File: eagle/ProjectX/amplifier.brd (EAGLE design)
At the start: 100 x 80 mm, 8 parts, among them U1 TC4427COA, U2 TC4427COA

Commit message: Some work on the final design
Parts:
- removed C3: 4.7uF, rcl:C0805
- removed C4: 100nF, rcl:C0805
- moved C2 15.1 mm to (72.7, 39.7)
- moved C1 14.3 mm to (72.7, 37.7)
- moved U1 5.63 mm to (74.8, 46.4), turned to 270 degrees
- moved SV2 5.47 mm to (53.3, 53.5)
- moved U2 2.55 mm to (71.6, 31.0), turned to 270 degrees
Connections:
- net GND: now also U1.1, U2.1; no longer C3.2, C4.2
- net VCC: now also U1.8, U2.8; no longer C3.1, C4.1
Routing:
- net N$4: track 21.4 -> 6.77 mm
- net GND: track 41.8 -> 29.7 mm
- net N$5: track 17.3 -> 6.77 mm
- net VCC: track 41.8 -> 31.3 mm
- net N$6: track 32.1 -> 22.9 mm
- net N$8: track 12.0 -> 3.35 mm
- net N$2: track 25.5 -> 19.5 mm
- net N$7: track 9.25 -> 3.35 mm
- net N$1: track 26.8 -> 22.4 mm
- net N$3: track 20.8 -> 19.5 mm

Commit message: More work on the 32 bit board
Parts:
- added C10, C12, C18, C20, C26, C28, C6: 100nF, rcl:C0805
- added C11, C17, C19, C25, C27, C5, C9: 4.7uF, rcl:C0805
- added U10, U11, U12, U17, U18, U19, U20, U25, U26, U27, U28, U5, U6, U9: TC4427COA, Microchip_By_element14_Batch_1:SOIC127P600X175-8N
- SV1, SV2: device con-lstb:MA20-2W -> Parts:MA20-2W
- moved U2 53.0 mm to (18.7, 32.0)
- moved C1 52.6 mm to (20.2, 40.5)
- moved C2 52.5 mm to (20.2, 38.5)
- moved U1 51.9 mm to (23.0, 46.2)
- moved SV1 9.36 mm to (59.3, 16.9)
- moved SV2 8.38 mm to (59.2, 59.4)
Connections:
- new net N$10: SV1.1, U2.7
- new net N$100: SV1.25, U26.7
- new net N$101: SV1.26, U26.5
- new net N$102: SV2.25, U26.2
- new net N$103: SV1.27, U25.7
- new net N$104: SV1.28, U25.5
- new net N$105: SV2.30, U27.4
- new net N$106: SV2.29, U27.2
- new net N$107: SV2.32, U28.4
- new net N$108: SV1.31, U28.7
- new net N$109: SV1.32, U28.5
- new net N$11: SV1.3, U1.7
- new net N$110: SV2.31, U28.2
- new net N$111: SV1.29, U27.7
- new net N$112: SV1.30, U27.5
- new net N$12: SV1.7, U6.7
- new net N$13: SV1.10, U10.5
- new net N$14: SV1.9, U10.7
- new net N$15: SV1.11, U9.7
- new net N$16: SV1.23, U20.7
- new net N$17: SV2.6, U5.4
- new net N$18: SV2.5, U5.2
- new net N$19: SV2.8, U6.4
- new net N$22: SV2.7, U6.2
- new net N$23: SV1.5, U5.7
- new net N$24: SV1.6, U5.5
- new net N$26: SV1.15, U12.7
- new net N$29: SV1.12, U9.5
- new net N$33: SV2.12, U9.4
- new net N$34: SV2.11, U9.2
- new net N$35: SV2.10, U10.4
- new net N$38: SV2.9, U10.2
- new net N$41: SV2.14, U11.4
- new net N$42: SV2.13, U11.2
- new net N$43: SV2.16, U12.4
- new net N$46: SV2.15, U12.2
- new net N$47: SV1.13, U11.7
- new net N$48: SV1.14, U11.5
- new net N$65: SV2.20, U17.4
- new net N$66: SV2.19, U17.2
- new net N$67: SV2.18, U18.4
- new net N$68: SV1.17, U18.7
- new net N$69: SV1.18, U18.5
- new net N$70: SV2.17, U18.2
- new net N$71: SV1.19, U17.7
- new net N$72: SV1.20, U17.5
- new net N$73: SV2.22, U19.4
- new net N$74: SV2.21, U19.2
- new net N$75: SV2.24, U20.4
- new net N$78: SV2.23, U20.2
- new net N$79: SV1.21, U19.7
- new net N$80: SV1.22, U19.5
- new net N$9: SV1.8, U6.5
- new net N$97: SV2.28, U25.4
- new net N$98: SV2.27, U25.2
- new net N$99: SV2.26, U26.4
- net GND: now also C10.2, C11.2, C12.2, C17.2, C18.2, C19.2, C20.2, C25.2, C26.2, C27.2, C28.2, C5.2, C6.2, C9.2, U10.1, U10.3, U11.1, U11.3, U12.1, U12.3, U17.1, U17.3, U18.1, U18.3, U19.1, U19.3, U20.1, U20.3, U25.1, U25.3, U26.1, U26.3, U27.1, U27.3, U28.1, U28.3, U5.1, U5.3, U6.1, U6.3, U9.1, U9.3; no longer SV1.1, SV1.2, SV2.1, SV2.2
- net N$1: now also SV2.2; no longer SV2.34
- net N$2: now also SV1.2, U2.5; no longer SV1.39, U1.7
- net N$3: now also SV1.4; no longer SV1.37
- net N$4: now also SV2.4; no longer SV2.38
- net N$5: now also SV2.3; no longer SV2.40
- net N$6: now also SV2.1; no longer SV2.36
- net N$7: now also SV1.16, U12.5; no longer SV1.35, U2.7
- net N$8: now also SV1.24, U20.5; no longer SV1.33, U2.5
- net VCC: now also C10.1, C11.1, C12.1, C17.1, C18.1, C19.1, C20.1, C25.1, C26.1, C27.1, C28.1, C5.1, C6.1, C9.1, U10.6, U10.8, U11.6, U11.8, U12.6, U12.8, U17.6, U17.8, U18.6, U18.8, U19.6, U19.8, U20.6, U20.8, U25.6, U25.8, U26.6, U26.8, U27.6, U27.8, U28.6, U28.8, U5.6, U5.8, U6.6, U6.8, U9.6, U9.8; no longer SV1.3, SV1.4, SV2.3, SV2.4
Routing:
- net GND: track 29.7 -> 333.3 mm
- net VCC: track 31.3 -> 321.0 mm
- net N$104: track 0.00 -> 40.6 mm
- net N$112: track 0.00 -> 40.3 mm
- net N$24: track 0.00 -> 38.9 mm
- net N$111: track 0.00 -> 38.0 mm
- net N$23: track 0.00 -> 37.1 mm
- net N$103: track 0.00 -> 36.6 mm
- net N$11: track 0.00 -> 34.7 mm
- net N$80: track 0.00 -> 32.6 mm
- net N$48: track 0.00 -> 32.0 mm
- net N$29: track 0.00 -> 31.5 mm
- net N$72: track 0.00 -> 31.3 mm
- net N$47: track 0.00 -> 30.3 mm
- net N$79: track 0.00 -> 29.6 mm
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
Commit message: Added a finished board
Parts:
- added D1: (no value), SparkFun-LED:LED-0603
- added J1, J2: (no value), SparkFun-Connectors:1X02_LONGPADS
- added R1: 1k, SparkFun-Resistors:0805
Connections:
- removed net VCC: C1.1, C10.1, C11.1, C12.1, C17.1, C18.1, C19.1, C2.1, C20.1, C25.1, C26.1, C27.1, C28.1, C5.1, C6.1, C9.1, U1.6, U1.8, U10.6, U10.8, U11.6, U11.8, U12.6, U12.8, U17.6, U17.8, U18.6, U18.8, U19.6, U19.8, U2.6, U2.8, U20.6, U20.8, U25.6, U25.8, U26.6, U26.8, U27.6, U27.8, U28.6, U28.8, U5.6, U5.8, U6.6, U6.8, U9.6, U9.8
- new net N$20: D1.A, R1.1
- new net VDD: C1.1, C10.1, C11.1, C12.1, C17.1, C18.1, C19.1, C2.1, C20.1, C25.1, C26.1, C27.1, C28.1, C5.1, C6.1, C9.1, J1.1, J2.1, R1.2, U1.6, U1.8, U10.6, U10.8, U11.6, U11.8, U12.6, U12.8, U17.6, U17.8, U18.6, U18.8, U19.6, U19.8, U2.6, U2.8, U20.6, U20.8, U25.6, U25.8, U26.6, U26.8, U27.6, U27.8, U28.6, U28.8, U5.6, U5.8, U6.6, U6.8, U9.6, U9.8
- net GND: now also D1.C, J1.2, J2.2, SV1.GND, SV1.GND+1, SV2.GND, SV2.GND+1
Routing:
- net VDD: track 0.00 -> 337.0 mm
- net VCC: track 321.0 -> 0.00 mm
- net N$1: track 14.0 -> 40.8 mm
- net N$4: track 0.00 -> 25.7 mm
- net N$107: track 16.7 -> 42.0 mm
- net N$6: track 15.0 -> 38.3 mm
- net N$105: track 0.00 -> 23.2 mm
- net N$110: track 15.7 -> 37.9 mm
- net N$106: track 0.00 -> 22.2 mm
- net N$17: track 0.00 -> 21.0 mm
- net N$5: track 0.00 -> 21.0 mm
- net N$97: track 0.00 -> 19.5 mm
- net N$98: track 0.00 -> 18.9 mm
- net N$99: track 14.0 -> 31.9 mm
- net N$18: track 0.00 -> 17.4 mm
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- added copper zone on layer 1, net GND
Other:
- board size 100 x 80 mm -> 93.6 x 54 mm

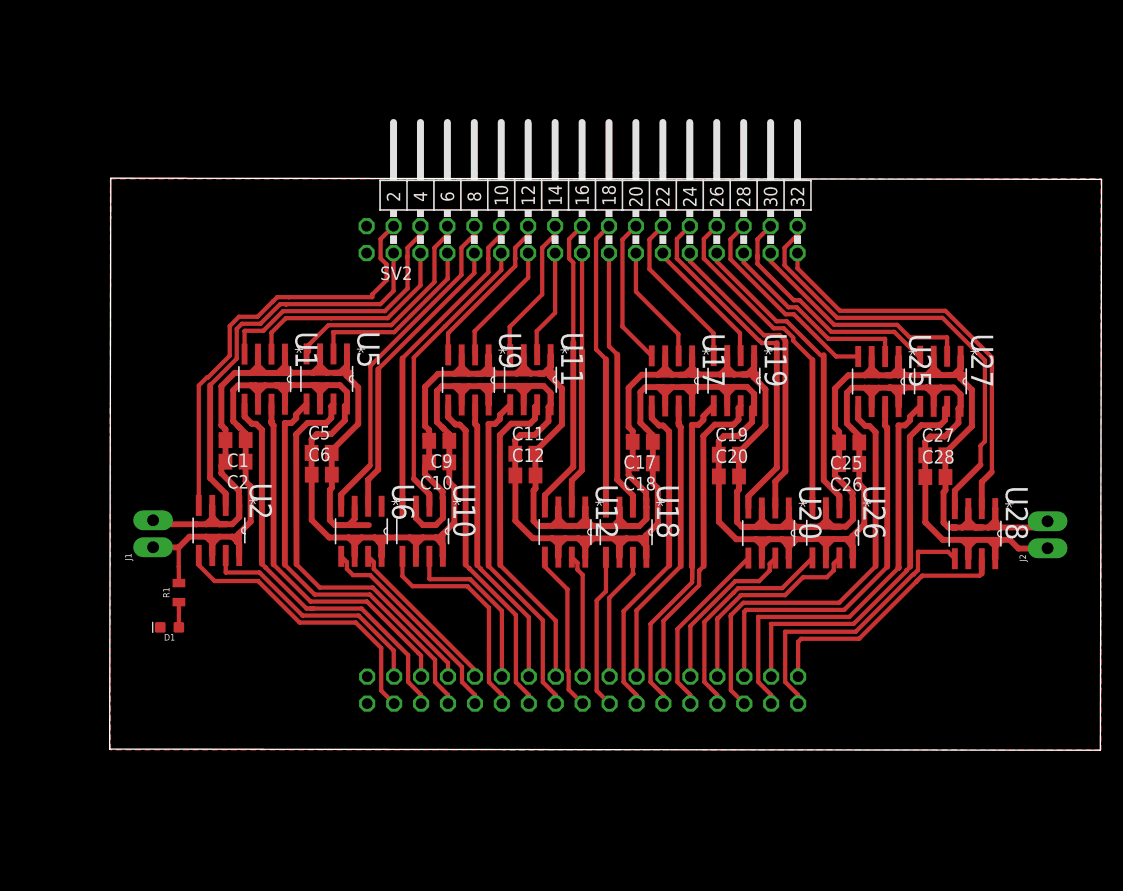
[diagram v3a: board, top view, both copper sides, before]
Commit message: Finished the small amplifier board
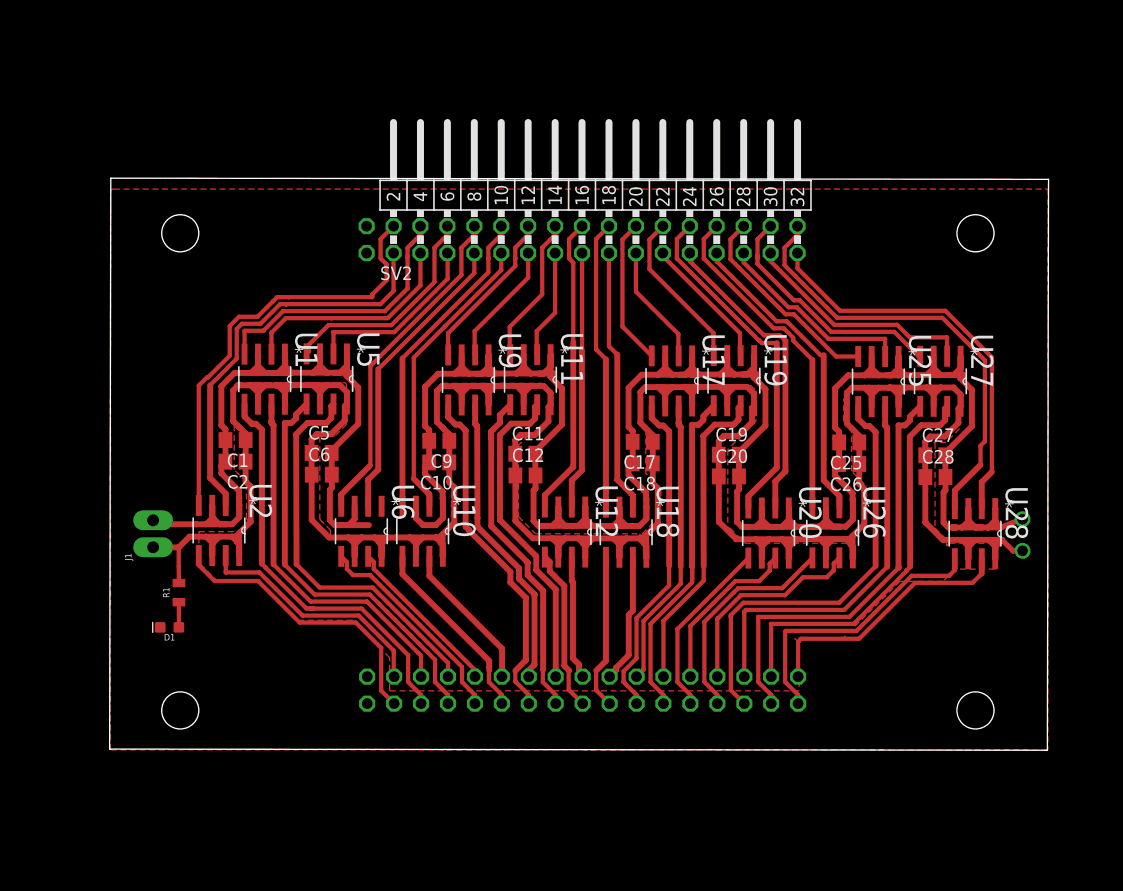
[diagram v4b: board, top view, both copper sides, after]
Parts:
- removed J2: (no value), SparkFun-Connectors:1X02_LONGPADS
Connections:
- net GND: no longer J2.2
- net VDD: no longer J2.1
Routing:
- net N$13: track 20.8 -> 18.1 mm
- net GND: track 329.1 -> 326.6 mm, vias 0 -> 1
- net VDD: track 337.0 -> 334.7 mm, vias 0 -> 1
- net N$14: track 16.4 -> 14.2 mm
- net N$109: track 27.7 -> 26.8 mm
- net N$29: track 31.5 -> 32.4 mm
- net N$48: track 32.0 -> 31.5 mm
- added copper zone on layer 1, net VDD
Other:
- board size 93.6 x 54 mm -> 88.6 x 54 mm

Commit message: changes
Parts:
- removed C10, C12, C18, C20, C26, C28, C6: 100nF, rcl:C0805
- removed C11, C17, C19, C25, C27, C5, C9: 4.7uF, rcl:C0805
- removed D1: (no value), SparkFun-LED:LED-0603
- removed J1: (no value), SparkFun-Connectors:1X02_LONGPADS
- removed R1: 1k, SparkFun-Resistors:0805
- removed U10, U11, U12, U17, U18, U19, U20, U25, U26, U27, U28, U5, U6, U9: TC4427COA, Microchip_By_element14_Batch_1:SOIC127P600X175-8N
- added C3: 4.7uF, rcl:C0805
- added C4: 100nF, rcl:C0805
- SV1, SV2: device Parts:MA20-2W -> con-lstb:MA20-2W
- moved C2 60.2 mm to (80.0, 45.7)
- moved C1 59.9 mm to (80.0, 43.4)
- moved U1 56.9 mm to (79.8, 50.0), turned to 0 degrees
- moved U2 54.9 mm to (72.4, 43.2), turned to 180 degrees
- moved SV1 9.36 mm to (53.3, 24.1)
- moved SV2 5.92 mm to (53.3, 58.9)
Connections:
- removed net N$10: SV1.1, U2.7
- removed net N$100: SV1.25, U26.7
- removed net N$101: SV1.26, U26.5
- removed net N$102: SV2.25, U26.2
- removed net N$103: SV1.27, U25.7
- removed net N$104: SV1.28, U25.5
- removed net N$105: SV2.30, U27.4
- removed net N$106: SV2.29, U27.2
- removed net N$107: SV2.32, U28.4
- removed net N$108: SV1.31, U28.7
- removed net N$109: SV1.32, U28.5
- removed net N$11: SV1.3, U1.7
- removed net N$110: SV2.31, U28.2
- removed net N$111: SV1.29, U27.7
- removed net N$112: SV1.30, U27.5
- removed net N$12: SV1.7, U6.7
- removed net N$13: SV1.10, U10.5
- removed net N$14: SV1.9, U10.7
- removed net N$15: SV1.11, U9.7
- removed net N$16: SV1.23, U20.7
- removed net N$17: SV2.6, U5.4
- removed net N$18: SV2.5, U5.2
- removed net N$19: SV2.8, U6.4
- removed net N$20: D1.A, R1.1
- removed net N$22: SV2.7, U6.2
- removed net N$23: SV1.5, U5.7
- removed net N$24: SV1.6, U5.5
- removed net N$26: SV1.15, U12.7
- removed net N$29: SV1.12, U9.5
- removed net N$33: SV2.12, U9.4
- removed net N$34: SV2.11, U9.2
- removed net N$35: SV2.10, U10.4
- removed net N$38: SV2.9, U10.2
- removed net N$41: SV2.14, U11.4
- removed net N$42: SV2.13, U11.2
- removed net N$43: SV2.16, U12.4
- removed net N$46: SV2.15, U12.2
- removed net N$47: SV1.13, U11.7
- removed net N$48: SV1.14, U11.5
- removed net N$65: SV2.20, U17.4
- removed net N$66: SV2.19, U17.2
- removed net N$67: SV2.18, U18.4
- removed net N$68: SV1.17, U18.7
- removed net N$69: SV1.18, U18.5
- removed net N$70: SV2.17, U18.2
- removed net N$71: SV1.19, U17.7
- removed net N$72: SV1.20, U17.5
- removed net N$73: SV2.22, U19.4
- removed net N$74: SV2.21, U19.2
- removed net N$75: SV2.24, U20.4
- removed net N$78: SV2.23, U20.2
- removed net N$79: SV1.21, U19.7
- removed net N$80: SV1.22, U19.5
- removed net N$9: SV1.8, U6.5
- removed net N$97: SV2.28, U25.4
- removed net N$98: SV2.27, U25.2
- removed net N$99: SV2.26, U26.4
- removed net VDD: C1.1, C10.1, C11.1, C12.1, C17.1, C18.1, C19.1, C2.1, C20.1, C25.1, C26.1, C27.1, C28.1, C5.1, C6.1, C9.1, J1.1, R1.2, U1.6, U1.8, U10.6, U10.8, U11.6, U11.8, U12.6, U12.8, U17.6, U17.8, U18.6, U18.8, U19.6, U19.8, U2.6, U2.8, U20.6, U20.8, U25.6, U25.8, U26.6, U26.8, U27.6, U27.8, U28.6, U28.8, U5.6, U5.8, U6.6, U6.8, U9.6, U9.8
- new net VCC: C1.1, C2.1, C3.1, C4.1, SV1.3, SV1.4, SV2.3, SV2.4, U1.6, U2.6
- net GND: now also C3.2, C4.2, SV1.1, SV1.2, SV2.1, SV2.2; no longer C10.2, C11.2, C12.2, C17.2, C18.2, C19.2, C20.2, C25.2, C26.2, C27.2, C28.2, C5.2, C6.2, C9.2, D1.C, J1.2, SV1.GND, SV1.GND+1, SV2.GND, SV2.GND+1, U1.1, U10.1, U10.3, U11.1, U11.3, U12.1, U12.3, U17.1, U17.3, U18.1, U18.3, U19.1, U19.3, U2.1, U20.1, U20.3, U25.1, U25.3, U26.1, U26.3, U27.1, U27.3, U28.1, U28.3, U5.1, U5.3, U6.1, U6.3, U9.1, U9.3
- net N$1: now also SV2.34; no longer SV2.2
- net N$2: now also SV1.39, U1.7; no longer SV1.2, U2.5
- net N$3: now also SV1.37; no longer SV1.4
- net N$4: now also SV2.38; no longer SV2.4
- net N$5: now also SV2.40; no longer SV2.3
- net N$6: now also SV2.36; no longer SV2.1
- net N$7: now also SV1.35, U2.7; no longer SV1.16, U12.5
- net N$8: now also SV1.33, U2.5; no longer SV1.24, U20.5
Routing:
- net VDD: track 334.7 -> 0.00 mm, vias 1 -> 0
- net GND: track 326.6 -> 0.00 mm, vias 1 -> 0
- net N$107: track 42.0 -> 0.00 mm
- net N$1: track 40.8 -> 0.00 mm
- net N$104: track 40.6 -> 0.00 mm
- net N$112: track 40.3 -> 0.00 mm
- net N$24: track 38.9 -> 0.00 mm
- net N$3: track 38.7 -> 0.00 mm
- net N$6: track 38.3 -> 0.00 mm
- net N$111: track 38.0 -> 0.00 mm
- net N$110: track 37.9 -> 0.00 mm
- net N$23: track 37.1 -> 0.00 mm
- net N$103: track 36.6 -> 0.00 mm
- net N$11: track 34.7 -> 0.00 mm
- net N$75: track 33.0 -> 0.00 mm
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- removed copper zone on layer 1, net GND
- removed copper zone on layer 1, net VDD
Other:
- board size 88.6 x 54 mm -> 100 x 80 mm

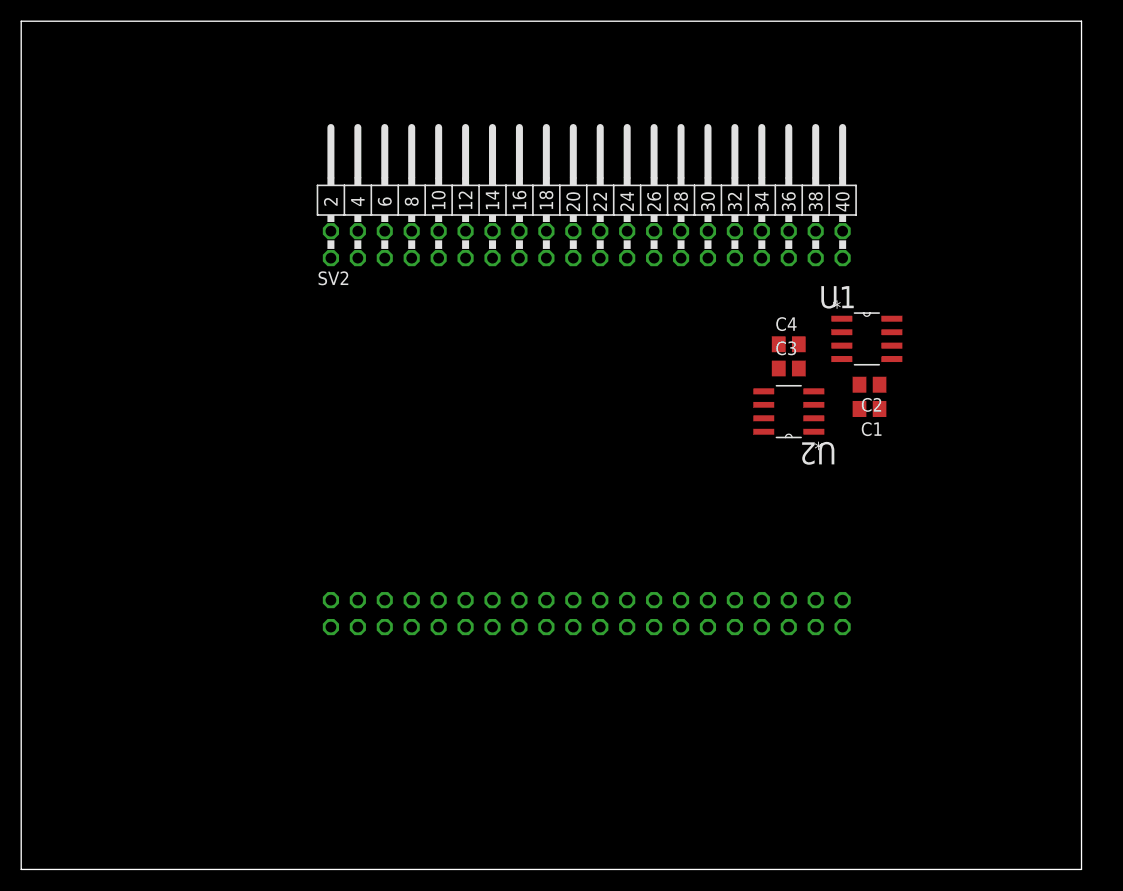
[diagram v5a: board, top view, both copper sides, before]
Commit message: Restored the eagle work to the last working copy
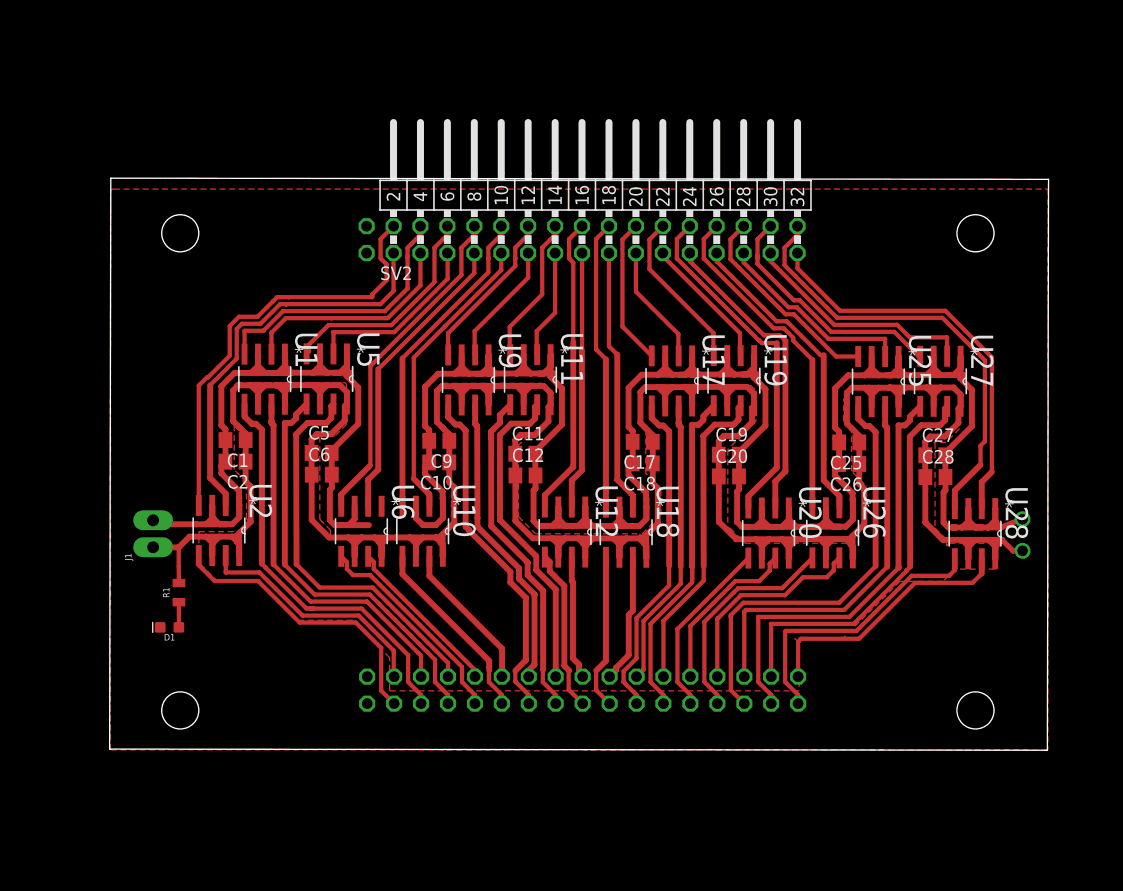
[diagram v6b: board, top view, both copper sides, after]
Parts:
- removed C3: 4.7uF, rcl:C0805
- removed C4: 100nF, rcl:C0805
- added C10, C12, C18, C20, C26, C28, C6: 100nF, rcl:C0805
- added C11, C17, C19, C25, C27, C5, C9: 4.7uF, rcl:C0805
- added D1: (no value), SparkFun-LED:LED-0603
- added J1: (no value), SparkFun-Connectors:1X02_LONGPADS
- added R1: 1k, SparkFun-Resistors:0805
- added U10, U11, U12, U17, U18, U19, U20, U25, U26, U27, U28, U5, U6, U9: TC4427COA, Microchip_By_element14_Batch_1:SOIC127P600X175-8N
- SV1, SV2: device con-lstb:MA20-2W -> Parts:MA20-2W
- moved C2 60.2 mm to (20.2, 38.5)
- moved C1 59.9 mm to (20.2, 40.5)
- moved U1 56.9 mm to (23.0, 46.2), turned to 270 degrees
- moved U2 54.9 mm to (18.7, 32.0), turned to 270 degrees
- moved SV1 9.36 mm to (59.3, 16.9)
- moved SV2 5.92 mm to (59.2, 59.4)
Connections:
- removed net VCC: C1.1, C2.1, C3.1, C4.1, SV1.3, SV1.4, SV2.3, SV2.4, U1.6, U2.6
- new net N$10: SV1.1, U2.7
- new net N$100: SV1.25, U26.7
- new net N$101: SV1.26, U26.5
- new net N$102: SV2.25, U26.2
- new net N$103: SV1.27, U25.7
- new net N$104: SV1.28, U25.5
- new net N$105: SV2.30, U27.4
- new net N$106: SV2.29, U27.2
- new net N$107: SV2.32, U28.4
- new net N$108: SV1.31, U28.7
- new net N$109: SV1.32, U28.5
- new net N$11: SV1.3, U1.7
- new net N$110: SV2.31, U28.2
- new net N$111: SV1.29, U27.7
- new net N$112: SV1.30, U27.5
- new net N$12: SV1.7, U6.7
- new net N$13: SV1.10, U10.5
- new net N$14: SV1.9, U10.7
- new net N$15: SV1.11, U9.7
- new net N$16: SV1.23, U20.7
- new net N$17: SV2.6, U5.4
- new net N$18: SV2.5, U5.2
- new net N$19: SV2.8, U6.4
- new net N$20: D1.A, R1.1
- new net N$22: SV2.7, U6.2
- new net N$23: SV1.5, U5.7
- new net N$24: SV1.6, U5.5
- new net N$26: SV1.15, U12.7
- new net N$29: SV1.12, U9.5
- new net N$33: SV2.12, U9.4
- new net N$34: SV2.11, U9.2
- new net N$35: SV2.10, U10.4
- new net N$38: SV2.9, U10.2
- new net N$41: SV2.14, U11.4
- new net N$42: SV2.13, U11.2
- new net N$43: SV2.16, U12.4
- new net N$46: SV2.15, U12.2
- new net N$47: SV1.13, U11.7
- new net N$48: SV1.14, U11.5
- new net N$65: SV2.20, U17.4
- new net N$66: SV2.19, U17.2
- new net N$67: SV2.18, U18.4
- new net N$68: SV1.17, U18.7
- new net N$69: SV1.18, U18.5
- new net N$70: SV2.17, U18.2
- new net N$71: SV1.19, U17.7
- new net N$72: SV1.20, U17.5
- new net N$73: SV2.22, U19.4
- new net N$74: SV2.21, U19.2
- new net N$75: SV2.24, U20.4
- new net N$78: SV2.23, U20.2
- new net N$79: SV1.21, U19.7
- new net N$80: SV1.22, U19.5
- new net N$9: SV1.8, U6.5
- new net N$97: SV2.28, U25.4
- new net N$98: SV2.27, U25.2
- new net N$99: SV2.26, U26.4
- new net VDD: C1.1, C10.1, C11.1, C12.1, C17.1, C18.1, C19.1, C2.1, C20.1, C25.1, C26.1, C27.1, C28.1, C5.1, C6.1, C9.1, J1.1, R1.2, U1.6, U1.8, U10.6, U10.8, U11.6, U11.8, U12.6, U12.8, U17.6, U17.8, U18.6, U18.8, U19.6, U19.8, U2.6, U2.8, U20.6, U20.8, U25.6, U25.8, U26.6, U26.8, U27.6, U27.8, U28.6, U28.8, U5.6, U5.8, U6.6, U6.8, U9.6, U9.8
- net GND: now also C10.2, C11.2, C12.2, C17.2, C18.2, C19.2, C20.2, C25.2, C26.2, C27.2, C28.2, C5.2, C6.2, C9.2, D1.C, J1.2, SV1.GND, SV1.GND+1, SV2.GND, SV2.GND+1, U1.1, U10.1, U10.3, U11.1, U11.3, U12.1, U12.3, U17.1, U17.3, U18.1, U18.3, U19.1, U19.3, U2.1, U20.1, U20.3, U25.1, U25.3, U26.1, U26.3, U27.1, U27.3, U28.1, U28.3, U5.1, U5.3, U6.1, U6.3, U9.1, U9.3; no longer C3.2, C4.2, SV1.1, SV1.2, SV2.1, SV2.2
- net N$1: now also SV2.2; no longer SV2.34
- net N$2: now also SV1.2, U2.5; no longer SV1.39, U1.7
- net N$3: now also SV1.4; no longer SV1.37
- net N$4: now also SV2.4; no longer SV2.38
- net N$5: now also SV2.3; no longer SV2.40
- net N$6: now also SV2.1; no longer SV2.36
- net N$7: now also SV1.16, U12.5; no longer SV1.35, U2.7
- net N$8: now also SV1.24, U20.5; no longer SV1.33, U2.5
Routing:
- net VDD: track 0.00 -> 334.7 mm, vias 0 -> 1
- net GND: track 0.00 -> 326.6 mm, vias 0 -> 1
- net N$107: track 0.00 -> 42.0 mm
- net N$1: track 0.00 -> 40.8 mm
- net N$104: track 0.00 -> 40.6 mm
- net N$112: track 0.00 -> 40.3 mm
- net N$24: track 0.00 -> 38.9 mm
- net N$3: track 0.00 -> 38.7 mm
- net N$6: track 0.00 -> 38.3 mm
- net N$111: track 0.00 -> 38.0 mm
- net N$110: track 0.00 -> 37.9 mm
- net N$23: track 0.00 -> 37.1 mm
- net N$103: track 0.00 -> 36.6 mm
- net N$11: track 0.00 -> 34.7 mm
- net N$75: track 0.00 -> 33.0 mm
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- added copper zone on layer 1, net GND
- added copper zone on layer 1, net VDD
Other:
- board size 100 x 80 mm -> 88.6 x 54 mm
